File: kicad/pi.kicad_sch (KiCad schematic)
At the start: 7 parts, among them J2 Raspberry Pi

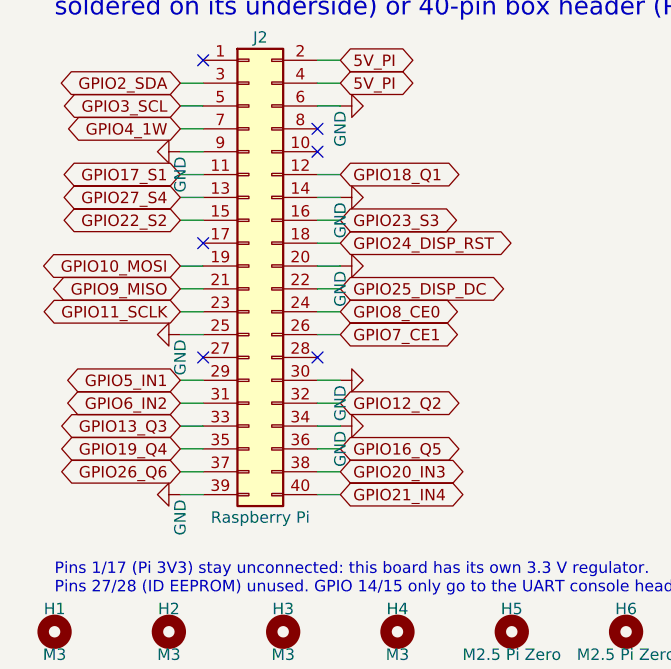
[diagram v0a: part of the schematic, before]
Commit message: kicad: strip obsolete v1 parts for v2 (SSR sheet, IN1..IN4, pH front end)
41 parts, their tracks/vias, pH guard zones, BNC keep-out and port silk removed; freed J2/U5 pins marked no-connect. ERC 0, DRC 0, parity 0; one expected +3V3 ratsnest to J24/JP3/J27/D28 left for the v2 layout.

Co-Authored-By: Claude Opus 5.5 <noreply@anthropic.com>
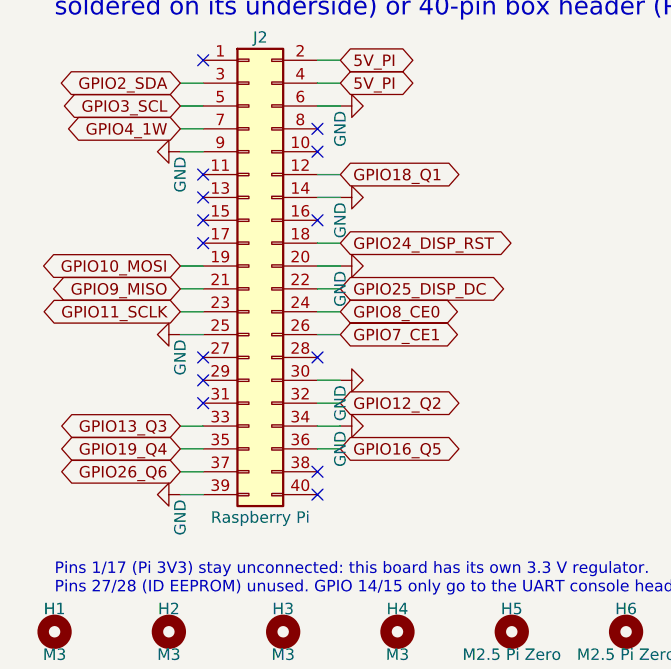
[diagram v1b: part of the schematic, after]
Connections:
- net GPIO17_S1: no longer names the net of J2.11 (Pin_11)
- net GPIO20_IN3: no longer names the net of J2.38 (Pin_38)
- net GPIO21_IN4: no longer names the net of J2.40 (Pin_40)
- net GPIO22_S2: no longer names the net of J2.15 (Pin_15)
- net GPIO23_S3: no longer names the net of J2.16 (Pin_16)
- net GPIO27_S4: no longer names the net of J2.13 (Pin_13)
- net GPIO5_IN1: no longer names the net of J2.29 (Pin_29)
- net GPIO6_IN2: no longer names the net of J2.31 (Pin_31)
- no-connect marks 6 -> 14

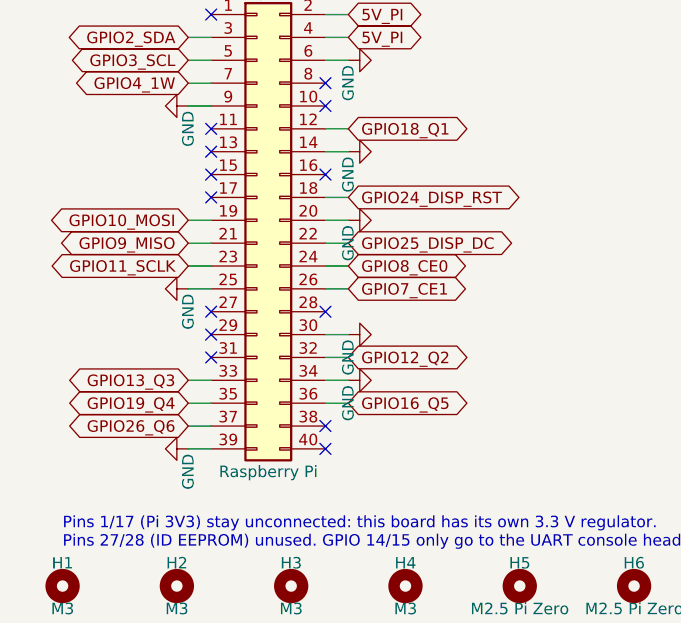
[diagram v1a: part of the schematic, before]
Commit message: kicad: v2 schematic and board update (PCA9685 x2, box-header ports, sensors, analog sockets)
New sheets pwm/powerbar/sensors; Q2/3/5/6 on PCA #1 ch 15-12; sensor GPIOs 5,6,20,21,22,23; 1-Wire +5V_EXT/Data/GND; four identical 0-5 V analog sockets; DC/LED/sensor ports as 2x4 box headers (pin n = Robo-Tank v3 RJ45 pin n). Board: 82 new footprints coarse-placed (56 parked beside the board), ERC 0, DRC copper 0, parity 0. README v2 plan updated.

Co-Authored-By: Claude Opus 5.5 <noreply@anthropic.com>
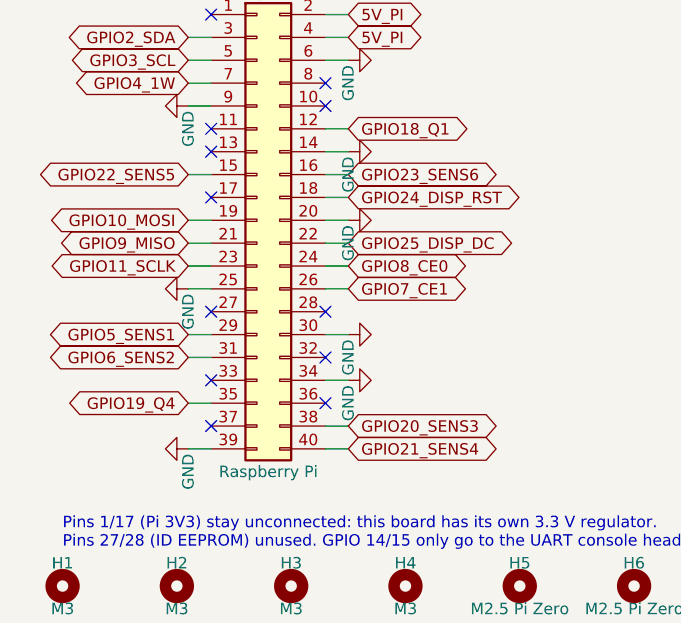
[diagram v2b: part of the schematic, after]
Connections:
- net GPIO22_SENS5: now reaches J2.15 (Pin_15)
- net GPIO23_SENS6: now reaches J2.16 (Pin_16)
- net GPIO5_SENS1: now reaches J2.29 (Pin_29)
- net GPIO6_SENS2: now reaches J2.31 (Pin_31)
- net GPIO20_SENS3: now reaches J2.38 (Pin_38)
- net GPIO21_SENS4: now reaches J2.40 (Pin_40)
- net GPIO12_Q2: no longer names the net of J2.32 (Pin_32)
- net GPIO13_Q3: no longer names the net of J2.33 (Pin_33)
- net GPIO16_Q5: no longer names the net of J2.36 (Pin_36)
- net GPIO26_Q6: no longer names the net of J2.37 (Pin_37)
- no-connect marks 14 -> 12
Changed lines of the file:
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@@
-	(wire
-		(pts
-			(xy 54.61 78.74) (xy 57.15 78.74)
-		)
-		(stroke
-			(width 0)
-			(type default)
-		)
-	)
 	(wire
 		(pts
@@
 	(wire
 		(pts
-			(xy 54.61 83.82) (xy 57.15 83.82)
-		)
-		(stroke
-			(width 0)
-			(type default)
-		)
-	)
-	(wire
-		(pts
-			(xy 41.91 81.28) (xy 39.37 81.28)
-		)
-		(stroke
-			(width 0)
-			(type default)
-		)
-	)
-	(wire
-		(pts
 			(xy 54.61 68.58) (xy 57.15 68.58)
 		)
@@
 	(wire
 		(pts
-			(xy 41.91 86.36) (xy 39.37 86.36)
-		)
-		(stroke
-			(width 0)
-			(type default)
-		)
-	)
-	(wire
-		(pts
 			(xy 41.91 83.82) (xy 39.37 83.82)
 		)
@@
 			(width 0)
 			(type default)
-		)
-	)
-	(global_label "GPIO13_Q3"
-		(shape bidirectional)
-		(at 39.37 81.28 180)
-		(fields_autoplaced yes)
-		(effects
-			(font
-				(size 1.27 1.27)
-			)
-			(justify right)
-		)
-		(property "Intersheetrefs" "${INTERSHEET_REFS}"
-			(at 39.37 81.28 0)
-			(hide yes)
-			(show_name no)
-			(do_not_autoplace no)
-			(effects
-				(font
-					(size 1.27 1.27)
-				)
-			)
 		)
 	)
@@
 		)
 	)
-	(global_label "GPIO26_Q6"
-		(shape bidirectional)
-		(at 39.37 86.36 180)
-		(fields_autoplaced yes)
-		(effects
-			(font
-				(size 1.27 1.27)
-			)
-			(justify right)
-		)
-		(property "Intersheetrefs" "${INTERSHEET_REFS}"
-			(at 39.37 86.36 0)
-			(hide yes)
-			(show_name no)
-			(do_not_autoplace no)
-			(effects
-				(font
-					(size 1.27 1.27)
-				)
-			)
-		)
-	)
 	(global_label "GPIO24_DISP_RST"
 		(shape bidirectional)
@@
 		)
 	)
-	(global_label "GPIO12_Q2"
-		(shape bidirectional)
-		(at 57.15 78.74 0)
-		(fields_autoplaced yes)
-		(effects
-			(font
-				(size 1.27 1.27)
-			)
-			(justify left)
-		)
-		(property "Intersheetrefs" "${INTERSHEET_REFS}"
-			(at 57.15 78.74 0)
-			(hide yes)
-			(show_name no)
-			(do_not_autoplace no)
-			(effects
-				(font
-					(size 1.27 1.27)
-				)
-			)
-		)
-	)
 	(global_label "5V_PI"
 		(shape bidirectional)
@@
 		(property "Intersheetrefs" "${INTERSHEET_REFS}"
 			(at 57.15 43.18 0)
-			(hide yes)
-			(show_name no)
-			(do_not_autoplace no)
-			(effects
-				(font
-					(size 1.27 1.27)
-				)
-			)
-		)
-	)
-	(global_label "GPIO16_Q5"
-		(shape bidirectional)
-		(at 57.15 83.82 0)
-		(fields_autoplaced yes)
-		(effects
-			(font
-				(size 1.27 1.27)
-			)
-			(justify left)
-		)
-		(property "Intersheetrefs" "${INTERSHEET_REFS}"
-			(at 57.15 83.82 0)
 			(hide yes)
 			(show_name no)
@@
 	)
 	(no_connect
-		(at 54.61 86.36)
-	)
-	(no_connect
-		(at 41.91 76.2)
-	)
-	(no_connect
-		(at 41.91 78.74)
-	)
-	(no_connect
 		(at 41.91 53.34)
-	)
-	(no_connect
-		(at 41.91 58.42)
-	)
-	(no_connect
-		(at 54.61 58.42)
 	)
 	(no_connect
@@
 	)
 	(no_connect
-		(at 54.61 88.9)
+		(at 54.61 78.74)
+	)
+	(no_connect
+		(at 41.91 81.28)
+	)
+	(no_connect
+		(at 54.61 83.82)
+	)
+	(no_connect
+		(at 41.91 86.36)
+	)
+	(wire
+		(pts
+			(xy 41.91 76.2) (xy 39.37 76.2)
+		)
+		(stroke
+			(width 0)
+			(type default)
+		)
+	)
+	(global_label "GPIO5_SENS1"
+		(shape bidirectional)
+		(at 39.37 76.2 180)
+		(fields_autoplaced yes)
+		(effects
+			(font
+				(size 1.27 1.27)
+			)
+			(justify right)
+		)
+		(property "Intersheetrefs" "${INTERSHEET_REFS}"
+			(at 39.37 76.2 0)
+			(effects
+				(font
+					(size 1.27 1.27)
+				)
+				(hide yes)
+			)
+		)
+	)
+	(wire
+		(pts
+			(xy 41.91 78.74) (xy 39.37 78.74)
+		)
+		(stroke
+			(width 0)
+			(type default)
+		)
+	)
+	(global_label "GPIO6_SENS2"
+		(shape bidirectional)
+		(at 39.37 78.74 180)
+		(fields_autoplaced yes)
+		(effects
+			(font
+				(size 1.27 1.27)
+			)
+			(justify right)
+		)
+		(property "Intersheetrefs" "${INTERSHEET_REFS}"
+			(at 39.37 78.74 0)
+			(effects
+				(font
+					(size 1.27 1.27)
+				)
+				(hide yes)
+			)
+		)
+	)
+	(wire
+		(pts
+			(xy 54.61 86.36) (xy 57.15 86.36)
+		)
+		(stroke
+			(width 0)
+			(type default)
+		)
+	)
+	(global_label "GPIO20_SENS3"
+		(shape bidirectional)
+		(at 57.15 86.36 0)
+		(fields_autoplaced yes)
+		(effects
+			(font
+				(size 1.27 1.27)
+			)
+			(justify left)
+		)
+		(property "Intersheetrefs" "${INTERSHEET_REFS}"
+			(at 57.15 86.36 0)
+			(effects
+				(font
+					(size 1.27 1.27)
+				)
+				(hide yes)
+			)
+		)
+	)
+	(wire
+		(pts
+			(xy 54.61 88.9) (xy 57.15 88.9)
+		)
+		(stroke
+			(width 0)
+			(type default)
+		)
+	)
+	(global_label "GPIO21_SENS4"
+		(shape bidirectional)
+		(at 57.15 88.9 0)
+		(fields_autoplaced yes)
+		(effects
+			(font
+				(size 1.27 1.27)
+			)
+			(justify left)
+		)
+		(property "Intersheetrefs" "${INTERSHEET_REFS}"
+			(at 57.15 88.9 0)
+			(effects
+				(font
+					(size 1.27 1.27)
+				)
+				(hide yes)
+			)
+		)
+	)
+	(wire
+		(pts
+			(xy 41.91 58.42) (xy 39.37 58.42)
+		)
+		(stroke
+			(width 0)
+			(type default)
+		)
+	)
+	(global_label "GPIO22_SENS5"
+		(shape bidirectional)
+		(at 39.37 58.42 180)
+		(fields_autoplaced yes)
+		(effects
+			(font
+				(size 1.27 1.27)
+			)
+			(justify right)
+		)
+		(property "Intersheetrefs" "${INTERSHEET_REFS}"
+			(at 39.37 58.42 0)
+			(effects
+				(font
+					(size 1.27 1.27)
+				)
+				(hide yes)
+			)
+		)
+	)
+	(wire
+		(pts
+			(xy 54.61 58.42) (xy 57.15 58.42)
+		)
+		(stroke
+			(width 0)
+			(type default)
+		)
+	)
+	(global_label "GPIO23_SENS6"
+		(shape bidirectional)
+		(at 57.15 58.42 0)
+		(fields_autoplaced yes)
+		(effects
+			(font
+				(size 1.27 1.27)
+			)
+			(justify left)
+		)
+		(property "Intersheetrefs" "${INTERSHEET_REFS}"
+			(at 57.15 58.42 0)
+			(effects
+				(font
+					(size 1.27 1.27)
+				)
+				(hide yes)
+			)
+		)
 	)
 )
